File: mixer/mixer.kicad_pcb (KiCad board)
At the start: 2 copper layers, 100 x 100 mm, 127 parts, among them J4 Conn_Coaxial, J5 Conn_Coaxial, J6 AudioJack3, J7 AudioJack3, P1 PMOD-Device-x2-Type-Generic-A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, T1 T-622, T2 Transformer_SP_1S, U10 OPA1602, U11 LM321, U12 4066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

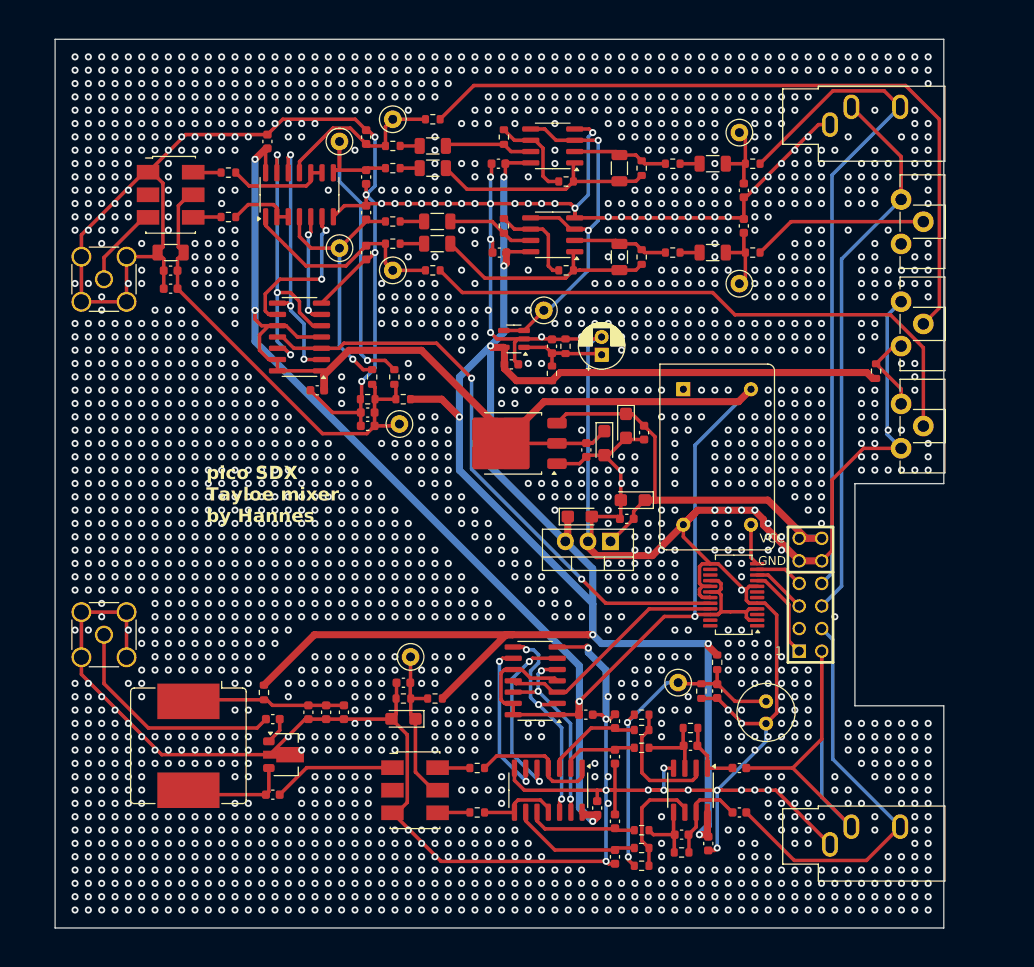
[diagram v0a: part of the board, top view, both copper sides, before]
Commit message: use lt1117 as linear voltage regulator
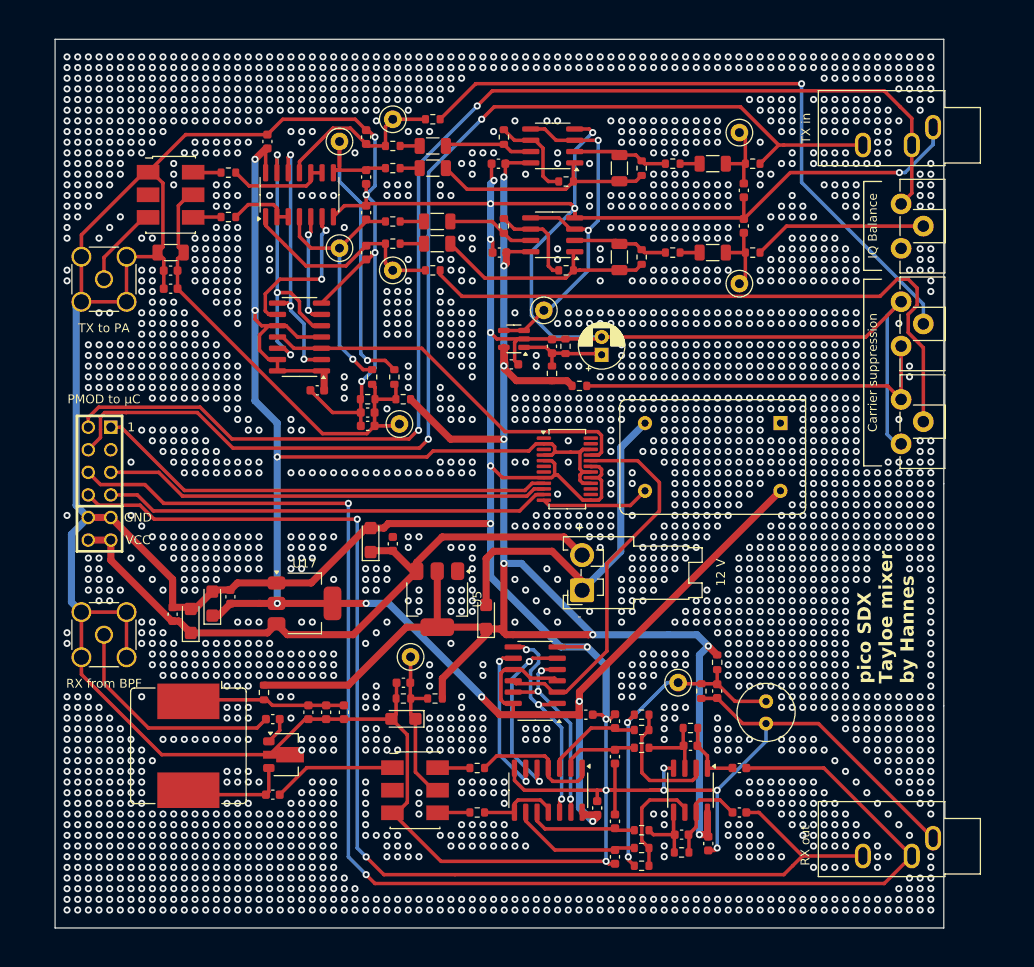
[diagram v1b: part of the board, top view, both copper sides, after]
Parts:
- added J1: Conn_01x02_Pin, Connector_JST:JST_VH_S2P-VH_1x02_P3.96mm_Horizontal, F.Cu at (135.0, 79.2)
- U17: value TLE4284 DV33 -> LT1117-3.3; footprint Package_TO_SOT_SMD:TO-252-3_TabPin2 -> Package_TO_SOT_SMD:SOT-223-3_TabPin2
- U5: value uA7805 -> LT1117-5.0; footprint Package_TO_SOT_THT:TO-220-3_Vertical -> Package_TO_SOT_SMD:SOT-223-3_TabPin2
- moved P1 81.0 mm to (80.7, 67.2), turned to 0 degrees
- moved C1 56.8 mm to (89.0, 81.9), turned to 90 degrees
- moved C3 53.7 mm to (91.0, 82.6), turned to 90 degrees
- moved C5 47.7 mm to (93.4, 80.7), turned to 90 degrees
- moved C7 43.3 mm to (95.5, 79.9), turned to 90 degrees
- moved R33 33.4 mm to (134.7, 56.2), turned to 0 degrees
- moved C4 29.8 mm to (111.2, 73.5), turned to 90 degrees
- moved U17 29.5 mm to (103.8, 80.7), turned to 0 degrees
- moved C2 26.5 mm to (113.7, 74.0), turned to 90 degrees
- moved U3 23.5 mm to (133.4, 65.6), turned to 0 degrees
- moved U5 20.6 mm to (118.7, 80.2), turned to -90 degrees
- moved C6 15.4 mm to (124.2, 82.2), turned to 90 degrees
- moved J6 11.6 mm to (174.5, 107.1), turned to -90 degrees
- moved J7 11.6 mm to (174.5, 27.1), turned to -90 degrees
- moved X8 11.6 mm to (157.4, 60.4), turned to 180 degrees
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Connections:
- P1 pad 10: TX_Q -> RX_Q
- P1 pad 7: RX_I -> TX_I
- P1 pad 8: RX_Q -> TX_Q
- P1 pad 9: TX_I -> RX_I
- U3 pad 20: TX_LO -> RX_LO
- U3 pad 21: RX_LO -> TX_LO
- U5 pad 1: +12V -> GND
- U5 pad 2: GND -> +5VA
- U5 pad 3: +5VA -> +12V
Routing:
- net GND: track 610.7 -> 750.0 mm, vias 2281 -> 2823
- net RX_I: track 50.2 -> 159.1 mm, vias 0 -> 2
- net RX_Q: track 47.1 -> 135.8 mm, vias 0 -> 2
- net TX_I: track 62.2 -> 140.9 mm, vias 0 -> 2
- net +5VA: track 253.3 -> 195.6 mm, vias 7 -> 8
- net TX_Q: track 77.2 -> 130.2 mm, vias 0 -> 2
- net SDA: track 5.38 -> 50.2 mm
- net SCL: track 6.17 -> 50.2 mm
- net INT: track 10.4 -> 52.0 mm
- net +3.3V: track 275.3 -> 238.2 mm, vias 5 -> 8
- net Net-(R33-Pad2): track 9.32 -> 42.0 mm
- net +12V: track 50.9 -> 74.4 mm
- net TX_LO: track 67.6 -> 44.3 mm, vias 2 -> 0
- net RX_LO: track 26.6 -> 43.1 mm
- net Net-(R35-Pad1): track 83.1 -> 75.0 mm, vias 0 -> 1
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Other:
- outline, holes or cut-outs redrawn
- board text added: "+"
- board text added: "-"
- board text added: "12 V"
- board text added: "Carrier suppression"
- board text added: "IQ Balance"
- board text added: "PMOD to µC"
- board text added: "RX from BPF"
- board text added: "RX out"
- board text added: "TX in"
- board text added: "TX to PA"

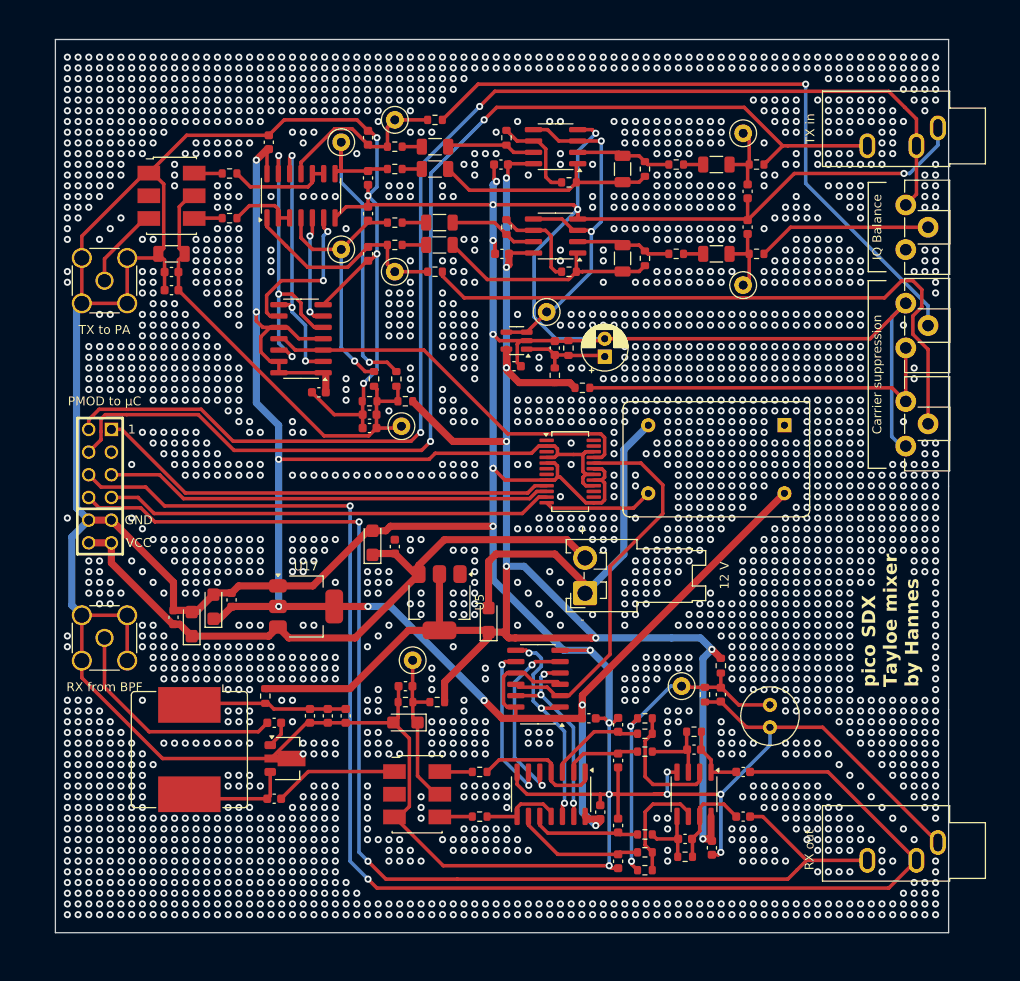
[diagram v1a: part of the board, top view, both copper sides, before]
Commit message: replace RF connectors, add missing silkscreen text
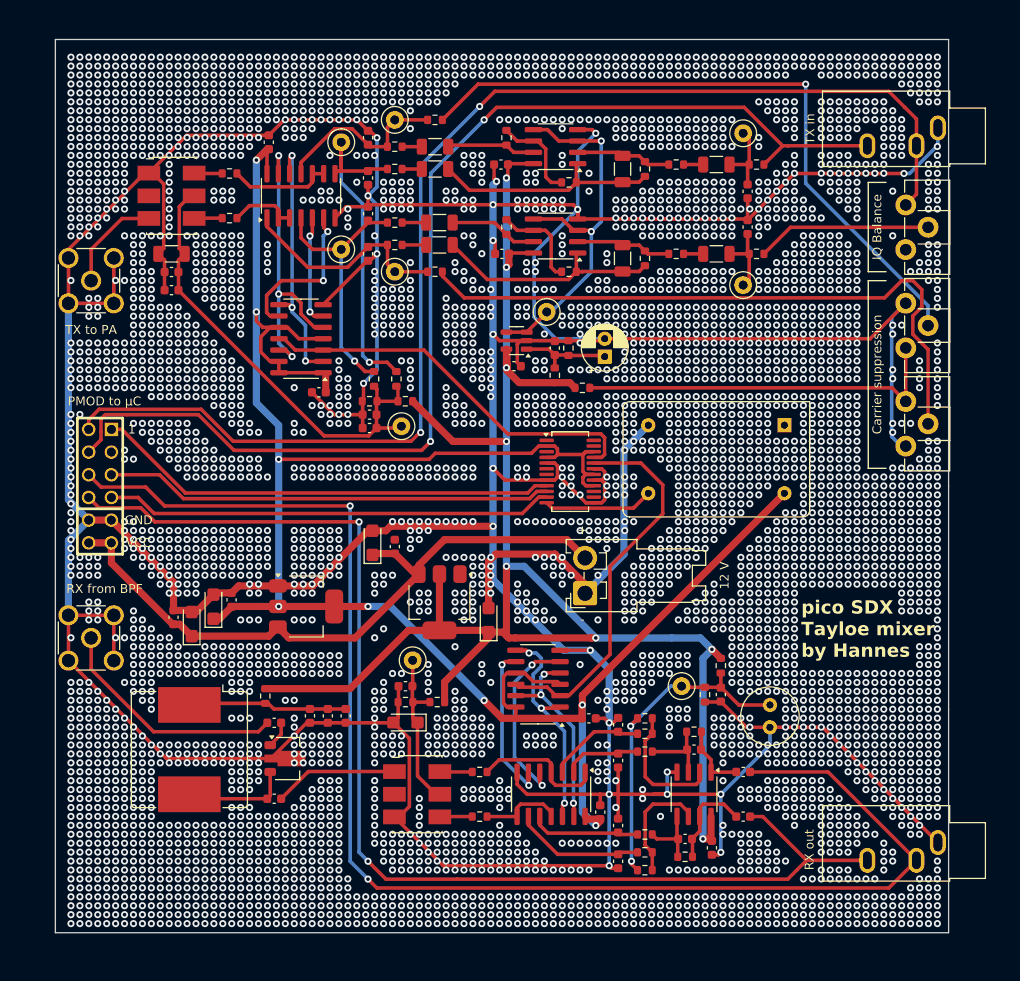
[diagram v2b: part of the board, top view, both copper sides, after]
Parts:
- J4, J5: footprint Connector_Coaxial:SMA_Amphenol_132291_Vertical -> Connector_Coaxial:SMA_Molex_73251-2200_Horizontal
- moved J4 1.50 mm to (79.7, 84.2), turned to 90 degrees
- moved J5 1.50 mm to (79.7, 44.2), turned to 90 degrees
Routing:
- net GND: track 750.0 -> 747.1 mm, vias 2823 -> 4814
- net /Upconverter/TX_OUT: track 9.27 -> 11.4 mm

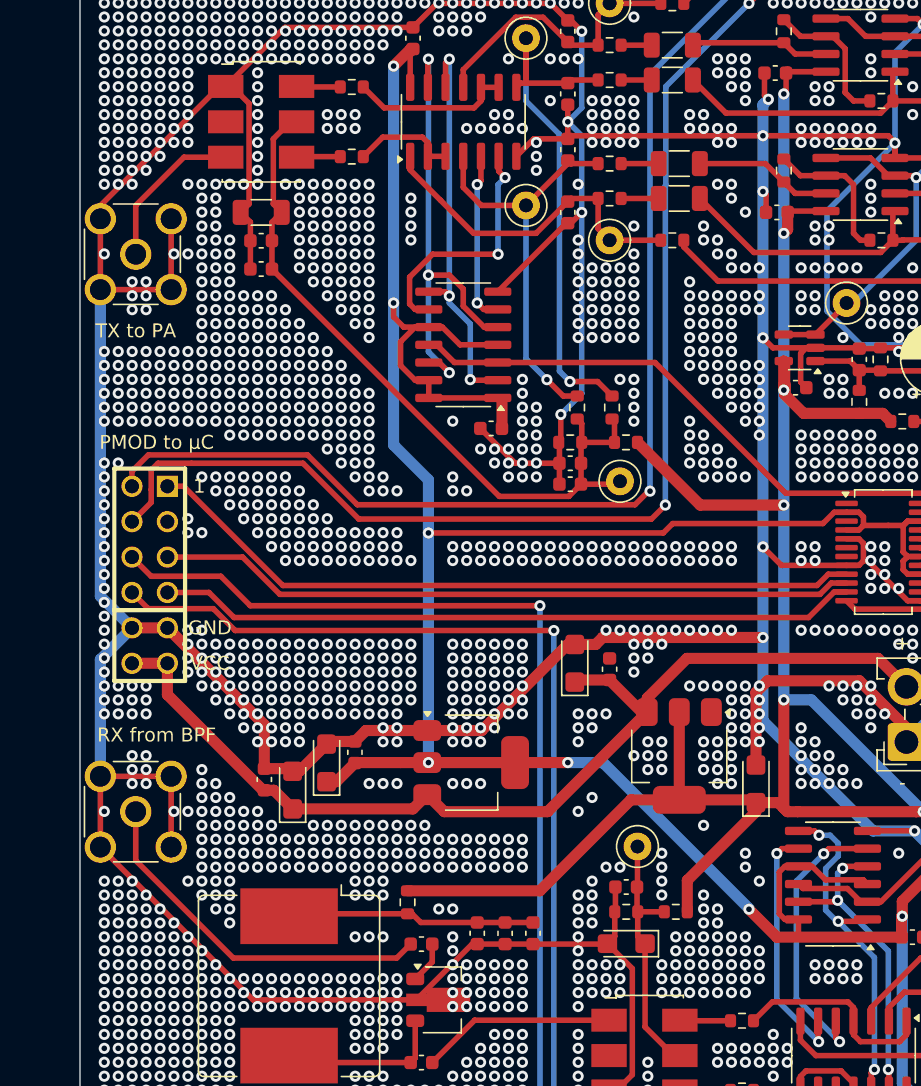
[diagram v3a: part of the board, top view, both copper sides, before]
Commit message: add gerber export settings and get drc-clean
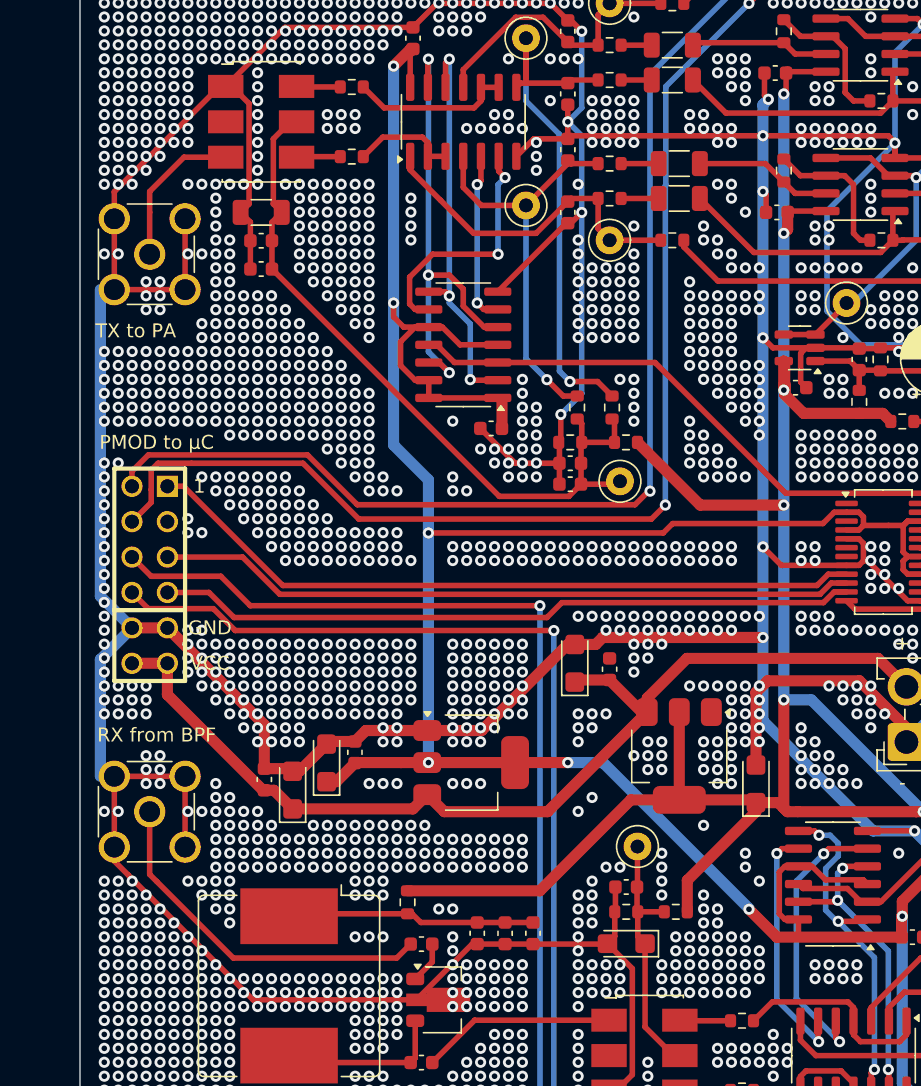
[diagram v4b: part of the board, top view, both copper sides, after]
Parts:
- moved J4 1.00 mm to (80.7, 84.2)
- moved J5 1.00 mm to (80.7, 44.2)
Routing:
- net GND: track 747.1 -> 746.3 mm, vias 4814 -> 4816
